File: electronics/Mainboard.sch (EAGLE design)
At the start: 225 parts, among them J1 JST_PH_B3B-PH-K-S(LF)(SN), J10 JST_PH_B3B-PH-K-S(LF)(SN), J11 JST_PH_B3B-PH-K-S(LF)(SN), J12 JST_PH_B3B-PH-K-S(LF)(SN), J13 JST_PH_B3B-PH-K-S(LF)(SN), J14 JST_PH_B3B-PH-K-S(LF)(SN), J15 JST_PH_B3B-PH-K-S(LF)(SN), J16 JST_PH_B3B-PH-K-S(LF)(SN), J17 JST_PH_B3B-PH-K-S(LF)(SN), J18 JST_PH_B3B-PH-K-S(LF)(SN), J19 JST_PH_B3B-PH-K-S(LF)(SN), J2 JST_PH_B3B-PH-K-S(LF)(SN), J20 JST_PH_B3B-PH-K-S(LF)(SN), J21 JST_PH_B3B-PH-K-S(LF)(SN), J22 JST_PH_B3B-PH-K-S(LF)(SN), J23 JST_PH_B3B-PH-K-S(LF)(SN), J24 JST_PH_B3B-PH-K-S(LF)(SN), J25 JST_PH_B3B-PH-K-S(LF)(SN), J26 JST_PH_B3B-PH-K-S(LF)(SN), J27 JST_PH_B3B-PH-K-S(LF)(SN), J28 JST_PH_B3B-PH-K-S(LF)(SN), J29 JST_PH_B3B-PH-K-S(LF)(SN), J3 JST_PH_B3B-PH-K-S(LF)(SN), J30 JST_PH_B3B-PH-K-S(LF)(SN), J31 JST_PH_B3B-PH-K-S(LF)(SN), J32 JST_PH_B3B-PH-K-S(LF)(SN), J33 B4B-PH-K-S(LF)(SN), J34 B4B-PH-K-S(LF)(SN), J35 B4B-PH-K-S(LF)(SN), J36 B4B-PH-K-S(LF)(SN), J37 B4B-PH-K-S(LF)(SN), J38 B4B-PH-K-S(LF)(SN), J39 B4B-PH-K-S(LF)(SN), J4 JST_PH_B3B-PH-K-S(LF)(SN), J40 B4B-PH-K-S(LF)(SN), J41 B4B-PH-K-S(LF)(SN), J42 B4B-PH-K-S(LF)(SN), J43 B4B-PH-K-S(LF)(SN), J44 B4B-PH-K-S(LF)(SN), J45 B4B-PH-K-S(LF)(SN), J46 B4B-PH-K-S(LF)(SN), J47 B4B-PH-K-S(LF)(SN), J48 B4B-PH-K-S(LF)(SN), J49 B4B-PH-K-S(LF)(SN), J5 JST_PH_B3B-PH-K-S(LF)(SN), J50 B4B-PH-K-S(LF)(SN), J51 B4B-PH-K-S(LF)(SN), J52 B4B-PH-K-S(LF)(SN), J53 B4B-PH-K-S(LF)(SN), J54 B4B-PH-K-S(LF)(SN), J55 B4B-PH-K-S(LF)(SN), J56 B4B-PH-K-S(LF)(SN), J57 B4B-PH-K-S(LF)(SN), J58 B4B-PH-K-S(LF)(SN), J59 B4B-PH-K-S(LF)(SN), J6 JST_PH_B3B-PH-K-S(LF)(SN), J60 B4B-PH-K-S(LF)(SN), J61 B4B-PH-K-S(LF)(SN), J62 B4B-PH-K-S(LF)(SN), J63 B4B-PH-K-S(LF)(SN), J64 B4B-PH-K-S(LF)(SN), J7 JST_PH_B3B-PH-K-S(LF)(SN), J8 JST_PH_B3B-PH-K-S(LF)(SN), J9 JST_PH_B3B-PH-K-S(LF)(SN), U1 AMP-5103309-7-34PIN_5103309-7, U15 AD5360BSTZ, U16 ADR425ARZ, U18 AD7730BRUZ, U19 AD5360BSTZ, U2 AMP-5103309-7-34PIN_5103309-7, U20 ADR425ARZ, U21 AD7730BRUZ, U22 STM32F103RCT6, U23 AD7730BRUZ, U24 AD7730BRUZ, U25 AD7730BRUZ, U26 AD7730BRUZ, U27 AD7730BRUZ, U28 AD7730BRUZ, U38 AD7730BRUZ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

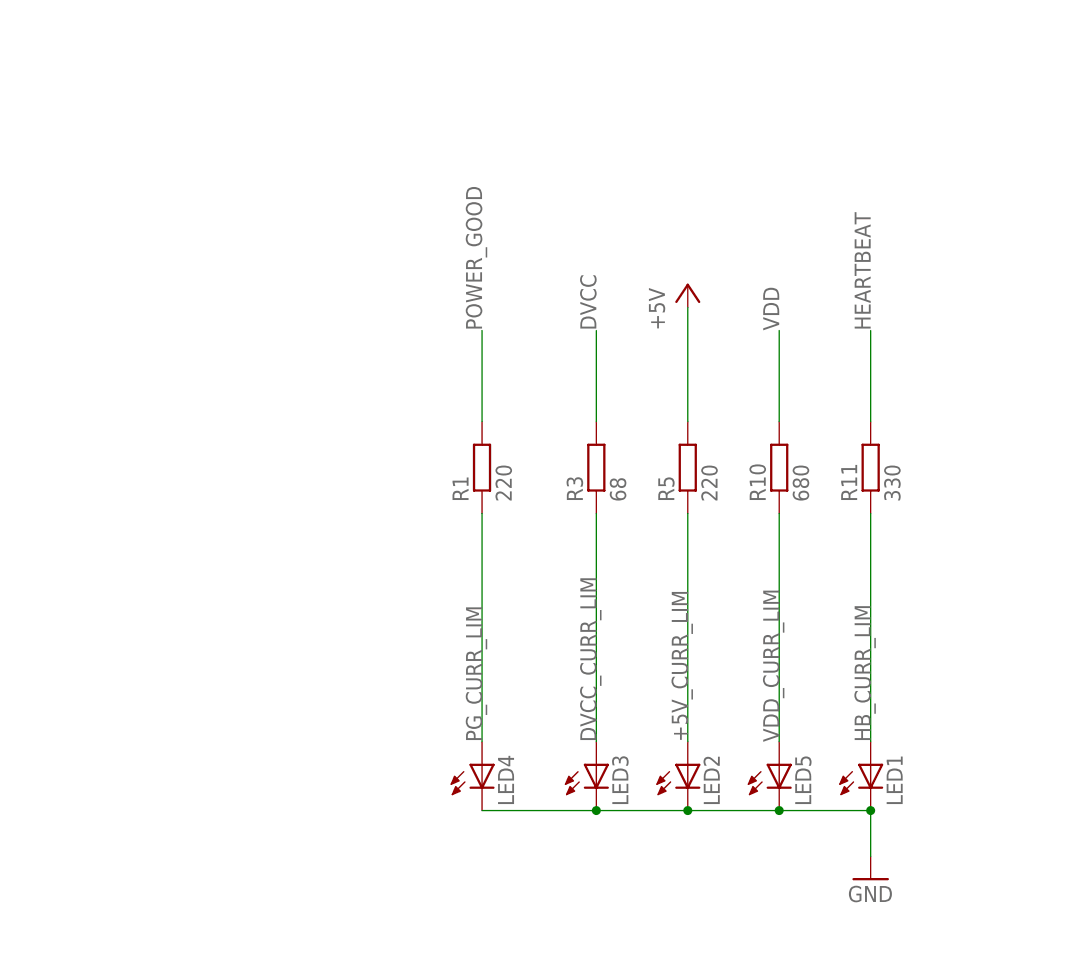
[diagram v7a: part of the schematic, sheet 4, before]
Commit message: reworked vias
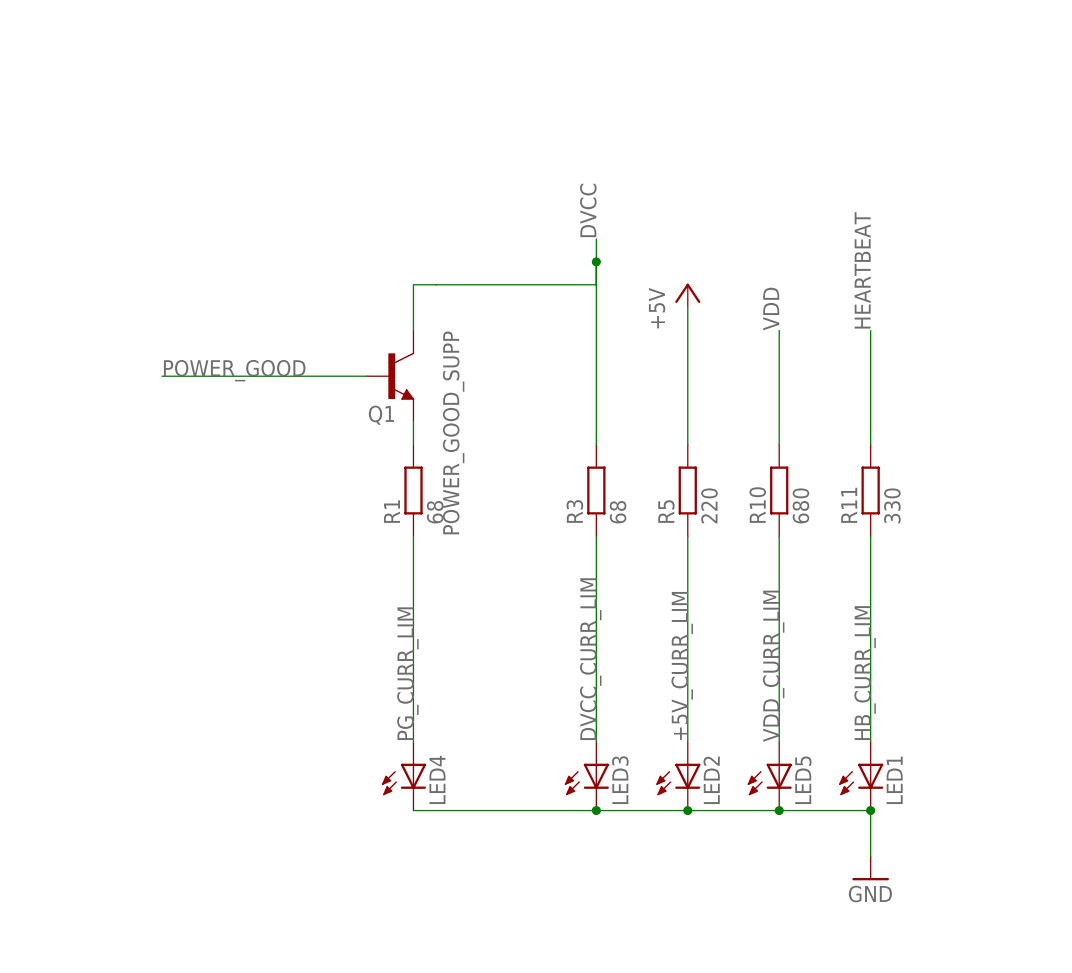
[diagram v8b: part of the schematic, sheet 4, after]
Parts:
- added Q1: BCF29SMD, transistor-npn:BCF29SMD
- R1: value 220 -> 68
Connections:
- new net POWER_GOOD_SUPP: Q1.E, R1.2
- net DVCC: now also Q1.C
- net POWER_GOOD: now also Q1.B; no longer R1.2
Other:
- moved on the sheet: LED4, R1, R10, R11, R3, R5
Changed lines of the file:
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@@
 <part name="GND135" library="supply1" library_urn="urn:adsk.eagle:library:371" deviceset="GND" device=""/>
 <part name="GND136" library="supply1" library_urn="urn:adsk.eagle:library:371" deviceset="GND" device=""/>
-<part name="R1" library="resistor" library_urn="urn:adsk.eagle:library:348" deviceset="R-EU_" device="R0805" package3d_urn="urn:adsk.eagle:package:26059/1" value="220"/>
+<part name="R1" library="resistor" library_urn="urn:adsk.eagle:library:348" deviceset="R-EU_" device="R0805" package3d_urn="urn:adsk.eagle:package:26059/1" value="68"/>
 <part name="R3" library="resistor" library_urn="urn:adsk.eagle:library:348" deviceset="R-EU_" device="R0805" package3d_urn="urn:adsk.eagle:package:26059/1" value="68"/>
 <part name="R5" library="resistor" library_urn="urn:adsk.eagle:library:348" deviceset="R-EU_" device="R0805" package3d_urn="urn:adsk.eagle:package:26059/1" value="220"/>
@@
 <part name="LED3" library="led" library_urn="urn:adsk.eagle:library:259" deviceset="LED" device="CHIP-LED0603" package3d_urn="urn:adsk.eagle:package:15819/3"/>
 <part name="LED4" library="led" library_urn="urn:adsk.eagle:library:259" deviceset="LED" device="CHIP-LED0603" package3d_urn="urn:adsk.eagle:package:15819/3"/>
+<part name="Q1" library="transistor-npn" library_urn="urn:adsk.eagle:library:398" deviceset="BCF29*" device="SMD" package3d_urn="urn:adsk.eagle:package:28990/2" value=""/>
 </parts>
 <sheets>
@@
 <instance part="GND135" gate="1" x="431.8" y="254"/>
 <instance part="GND136" gate="1" x="355.6" y="218.44"/>
-<instance part="R1" gate="G$1" x="312.42" y="264.16" rot="R90"/>
-<instance part="R3" gate="G$1" x="325.12" y="264.16" rot="R90"/>
-<instance part="R5" gate="G$1" x="335.28" y="264.16" rot="R90"/>
-<instance part="R10" gate="G$1" x="345.44" y="264.16" rot="R90"/>
+<instance part="R1" gate="G$1" x="304.8" y="261.62" rot="R90"/>
+<instance part="R3" gate="G$1" x="325.12" y="261.62" rot="R90"/>
+<instance part="R5" gate="G$1" x="335.28" y="261.62" rot="R90"/>
+<instance part="R10" gate="G$1" x="345.44" y="261.62" rot="R90"/>
 <instance part="P+54" gate="1" x="335.28" y="284.48"/>
 <instance part="JP1" gate="A" x="30.48" y="213.36"/>
@@
 <instance part="X1" gate="-3" x="116.84" y="259.08"/>
 <instance part="GND150" gate="1" x="104.14" y="254"/>
-<instance part="R11" gate="G$1" x="355.6" y="264.16" rot="R90"/>
+<instance part="R11" gate="G$1" x="355.6" y="261.62" rot="R90"/>
 <instance part="LED1" gate="G$1" x="355.6" y="231.14"/>
 <instance part="LED5" gate="G$1" x="345.44" y="231.14"/>
 <instance part="LED2" gate="G$1" x="335.28" y="231.14"/>
 <instance part="LED3" gate="G$1" x="325.12" y="231.14"/>
-<instance part="LED4" gate="G$1" x="312.42" y="231.14"/>
+<instance part="LED4" gate="G$1" x="304.8" y="231.14"/>
+<instance part="Q1" gate="G$1" x="302.26" y="274.32" smashed="yes">
+<attribute name="NAME" x="299.72" y="269.24" size="1.778" layer="95"/>
+<attribute name="VALUE" x="292.1" y="279.4" size="1.778" layer="96"/>
+</instance>
 </instances>
 <busses>
@@
 <segment>
 <pinref part="R3" gate="G$1" pin="2"/>
-<wire x1="325.12" y1="269.24" x2="325.12" y2="279.4" width="0.1524" layer="91"/>
-<label x="325.12" y="279.4" size="1.778" layer="95" rot="R90"/>
+<wire x1="325.12" y1="266.7" x2="325.12" y2="284.48" width="0.1524" layer="91"/>
+<label x="325.12" y="289.56" size="1.778" layer="95" rot="R90"/>
+<wire x1="325.12" y1="284.48" x2="325.12" y2="287.02" width="0.1524" layer="91"/>
+<wire x1="325.12" y1="287.02" x2="325.12" y2="289.56" width="0.1524" layer="91"/>
+<wire x1="325.12" y1="287.02" x2="325.12" y2="284.48" width="0.1524" layer="91"/>
+<wire x1="325.12" y1="284.48" x2="307.34" y2="284.48" width="0.1524" layer="91"/>
+<junction x="325.12" y="287.02"/>
+<pinref part="Q1" gate="G$1" pin="C"/>
+<wire x1="307.34" y1="284.48" x2="304.8" y2="284.48" width="0.1524" layer="91"/>
+<wire x1="304.8" y1="284.48" x2="304.8" y2="279.4" width="0.1524" layer="91"/>
 </segment>
 </net>
@@
 <segment>
 <pinref part="R5" gate="G$1" pin="2"/>
-<wire x1="335.28" y1="269.24" x2="335.28" y2="281.94" width="0.1524" layer="91"/>
+<wire x1="335.28" y1="266.7" x2="335.28" y2="281.94" width="0.1524" layer="91"/>
 <pinref part="P+54" gate="1" pin="+5V"/>
 </segment>
@@
 <segment>
 <pinref part="R10" gate="G$1" pin="2"/>
-<wire x1="345.44" y1="269.24" x2="345.44" y2="279.4" width="0.1524" layer="91"/>
+<wire x1="345.44" y1="266.7" x2="345.44" y2="279.4" width="0.1524" layer="91"/>
 <label x="345.44" y="279.4" size="1.778" layer="95" rot="R90"/>
 </segment>
@@
 </segment>
 <segment>
-<wire x1="312.42" y1="226.06" x2="325.12" y2="226.06" width="0.1524" layer="91"/>
+<wire x1="304.8" y1="226.06" x2="325.12" y2="226.06" width="0.1524" layer="91"/>
 <wire x1="325.12" y1="226.06" x2="335.28" y2="226.06" width="0.1524" layer="91"/>
 <wire x1="335.28" y1="226.06" x2="345.44" y2="226.06" width="0.1524" layer="91"/>
@@
 </segment>
 <segment>
-<pinref part="R1" gate="G$1" pin="2"/>
-<wire x1="312.42" y1="269.24" x2="312.42" y2="279.4" width="0.1524" layer="91"/>
-<label x="312.42" y="279.4" size="1.778" layer="95" rot="R90"/>
+<pinref part="Q1" gate="G$1" pin="B"/>
+<wire x1="299.72" y1="274.32" x2="276.86" y2="274.32" width="0.1524" layer="91"/>
+<label x="276.86" y="274.32" size="1.778" layer="95"/>
 </segment>
 </net>
@@
 <segment>
 <pinref part="R1" gate="G$1" pin="1"/>
-<wire x1="312.42" y1="233.68" x2="312.42" y2="259.08" width="0.1524" layer="91"/>
-<label x="312.42" y="233.68" size="1.778" layer="95" rot="R90"/>
+<wire x1="304.8" y1="233.68" x2="304.8" y2="256.54" width="0.1524" layer="91"/>
+<label x="304.8" y="233.68" size="1.778" layer="95" rot="R90"/>
 <pinref part="LED4" gate="G$1" pin="A"/>
 </segment>
@@
 <segment>
 <pinref part="R3" gate="G$1" pin="1"/>
-<wire x1="325.12" y1="233.68" x2="325.12" y2="259.08" width="0.1524" layer="91"/>
+<wire x1="325.12" y1="233.68" x2="325.12" y2="256.54" width="0.1524" layer="91"/>
 <label x="325.12" y="233.68" size="1.778" layer="95" rot="R90"/>
 <pinref part="LED3" gate="G$1" pin="A"/>
@@
 <segment>
 <pinref part="R5" gate="G$1" pin="1"/>
-<wire x1="335.28" y1="233.68" x2="335.28" y2="259.08" width="0.1524" layer="91"/>
+<wire x1="335.28" y1="233.68" x2="335.28" y2="256.54" width="0.1524" layer="91"/>
 <label x="335.28" y="233.68" size="1.778" layer="95" rot="R90"/>
 <pinref part="LED2" gate="G$1" pin="A"/>
@@
 <segment>
 <pinref part="R10" gate="G$1" pin="1"/>
-<wire x1="345.44" y1="233.68" x2="345.44" y2="259.08" width="0.1524" layer="91"/>
+<wire x1="345.44" y1="233.68" x2="345.44" y2="256.54" width="0.1524" layer="91"/>
 <label x="345.44" y="233.68" size="1.778" layer="95" rot="R90"/>
 <pinref part="LED5" gate="G$1" pin="A"/>
@@
 <segment>
 <pinref part="R11" gate="G$1" pin="1"/>
-<wire x1="355.6" y1="233.68" x2="355.6" y2="259.08" width="0.1524" layer="91"/>
+<wire x1="355.6" y1="233.68" x2="355.6" y2="256.54" width="0.1524" layer="91"/>
 <label x="355.6" y="233.68" size="1.778" layer="95" rot="R90"/>
 <pinref part="LED1" gate="G$1" pin="A"/>
@@
 <segment>
 <pinref part="R11" gate="G$1" pin="2"/>
-<wire x1="355.6" y1="269.24" x2="355.6" y2="279.4" width="0.1524" layer="91"/>
+<wire x1="355.6" y1="266.7" x2="355.6" y2="279.4" width="0.1524" layer="91"/>
 <label x="355.6" y="279.4" size="1.778" layer="95" rot="R90"/>
 </segment>
@@
 </segment>
 </net>
+<net name="POWER_GOOD_SUPP" class="0">
+<segment>
+<pinref part="R1" gate="G$1" pin="2"/>
+<pinref part="Q1" gate="G$1" pin="E"/>
+<wire x1="304.8" y1="266.7" x2="304.8" y2="269.24" width="0.1524" layer="91"/>
+<label x="309.88" y="256.54" size="1.778" layer="95" rot="R90"/>
+</segment>
+</net>
